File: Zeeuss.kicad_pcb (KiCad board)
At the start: 2 copper layers, 20 x 18 mm, 30 parts, among them J2 Conn_01x05_Male, SW1 SW_SPST, U1 MP20045, U2 IP5306

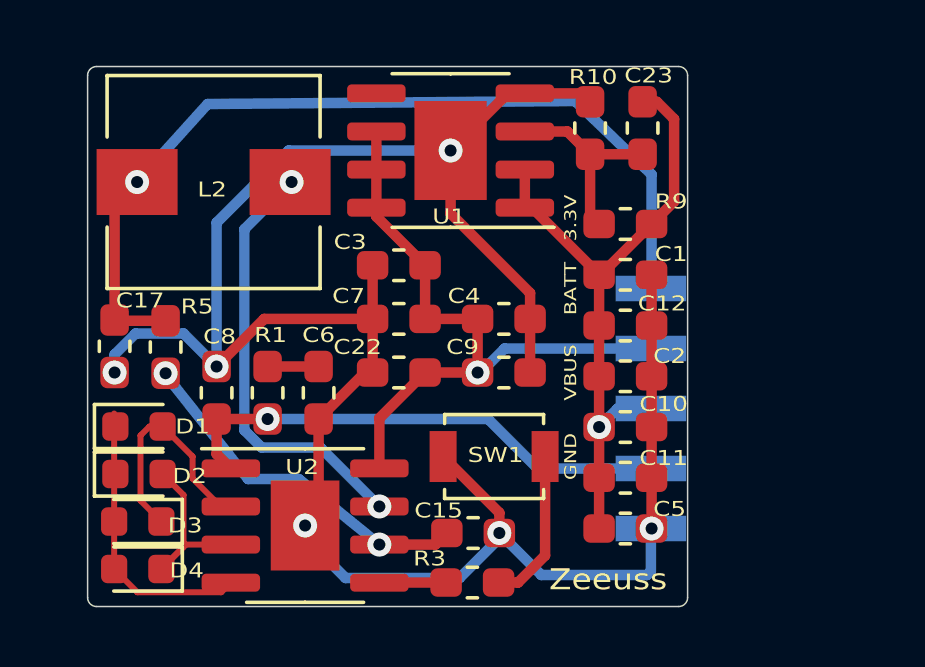
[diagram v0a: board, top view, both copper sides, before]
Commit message: 2.0版本，删掉一些滤波电容，引出充电led引脚，取消自带led，引出开关，利用单片机控制开关，PCB重新布局
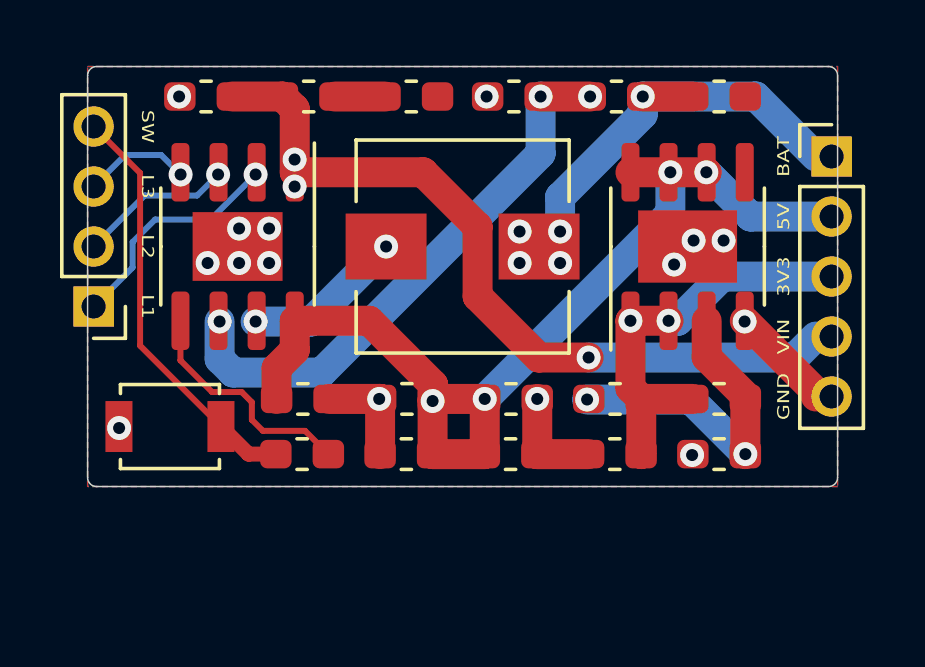
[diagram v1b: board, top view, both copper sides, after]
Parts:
- removed C1, C10, C2, C5: 100nf, Capacitor_SMD:C_0603_1608Metric_Pad1.05x0.95mm_HandSolder
- removed C12: 10uf, Capacitor_SMD:C_0603_1608Metric_Pad1.05x0.95mm_HandSolder
- removed D1, D2, D3, D4: SMT_LED, LED_SMD:LED_0603_1608Metric
- added J1: Conn_01x05_Female, Connector_PinHeader_2.00mm:PinHeader_1x05_P2.00mm_Vertical, F.Cu at (124.8, 103.0)
- C11, C22: value 2.2uf -> 2.2uF
- C15, C17, C3, C4, C7, C9: value 22uf -> 22uF
- C23: value 100pf -> 0.1uF
- C8: value 10uf -> 10uF
- J2: value Conn_01x05_Male -> Conn_01x04_Female; footprint Connector_PinHeader_2.00mm:PinHeader_1x05_P2.00mm_Vertical_SMD_Pin1Right -> Connector_PinHeader_2.00mm:PinHeader_1x04_P2.00mm_Vertical; moved to F.Cu
- moved C17 21.8 mm to (121.0, 101.0), turned to 0 degrees
- moved J2 17.7 mm to (100.2, 108.0), turned to 180 degrees
- moved R5 17.2 mm to (117.6, 101.0), turned to 180 degrees
- moved C15 14.6 mm to (114.2, 101.0), turned to 180 degrees
- moved R10 11.7 mm to (121.0, 112.9), turned to 0 degrees
- moved SW1 10.9 mm to (102.7, 112.0), turned to 0 degrees
- moved C6 10.3 mm to (110.8, 101.0), turned to 0 degrees
- moved R1 9.97 mm to (107.4, 101.0), turned to 0 degrees
- moved C8 9.88 mm to (104.0, 101.0), turned to 180 degrees
- moved U2 9.57 mm to (105.0, 106.0), turned to 270 degrees
- moved C23 9.38 mm to (121.0, 111.1), turned to 0 degrees
- moved L2 8.57 mm to (112.5, 106.0), turned to 0 degrees
- moved U1 8.52 mm to (120.0, 106.0), turned to 90 degrees
- moved C4 7.21 mm to (107.2, 111.1)
- moved R3 7.11 mm to (107.2, 112.9), turned to 180 degrees
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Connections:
- J2 pad 1: Earth -> /LED1
- J2 pad 2: VBUS -> /LED2
- J2 pad 3: +3V3 -> /LED3
- J2 pad 4: +5V -> /SW
- R3 pad 2: Net-(R3-Pad2) -> /SW
- SW1 pad 1: Net-(R3-Pad2) -> Earth
- SW1 pad 2: Earth -> /SW
- U2 pad 2: Net-(D1-Pad2) -> /LED1
- U2 pad 3: Net-(D2-Pad2) -> /LED2
- U2 pad 4: Net-(D1-Pad1) -> /LED3
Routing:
- net Earth: track 75.1 -> 10.6 mm, vias 6 -> 15
- net +BATT: track 29.7 -> 13.9 mm, vias 1 -> 5
- net /SW: track 0.00 -> 13.9 mm
- net +5V: track 22.1 -> 32.9 mm, vias 1 -> 4
- net +3V3: track 22.9 -> 13.1 mm, vias 1 -> 2
- net Net-(D1-Pad1): track 9.59 -> 0.00 mm
- net Net-(L2-Pad1): track 14.5 -> 5.39 mm
- net VBUS: track 17.0 -> 25.9 mm, vias 1 -> 3
- net Net-(D1-Pad2): track 7.82 -> 0.00 mm
- net /LED1: track 0.00 -> 7.67 mm, vias 0 -> 1
- net Net-(C15-Pad1): track 12.0 -> 18.7 mm, vias 2 -> 3
- net Net-(D2-Pad2): track 6.41 -> 0.00 mm
- net Net-(R3-Pad1): track 2.23 -> 7.89 mm
- net Net-(R3-Pad2): track 5.22 -> 0.00 mm
- net /LED2: track 0.00 -> 5.09 mm, vias 0 -> 1
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- added copper zone on B.Cu, net Earth
- added copper zone on F.Cu, net Earth
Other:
- board size 20 x 18 mm -> 25 x 14 mm
- board text added: "3V3"
- board text added: "5V"
- board text added: "BAT"
- board text added: "L1"
- board text added: "L2"
- board text added: "L3"
- board text added: "SW"
- board text added: "VIN"
- board text removed: "3.3V"
- board text removed: "BATT"
- board text removed: "VBUS"
- board text removed: "Zeeuss"

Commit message: 更新文档，gerber
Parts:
- added G***: LOGO, Logo:logo, B.Cu at (112.5, 106.7)
- moved J2 5.00 mm to (100.2, 103.0), turned to 0 degrees
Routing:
- net /SW: track 13.9 -> 8.30 mm
- net /LED3: track 3.55 -> 5.37 mm, vias 1 -> 0
- net /LED1: track 7.67 -> 7.00 mm, vias 1 -> 0
